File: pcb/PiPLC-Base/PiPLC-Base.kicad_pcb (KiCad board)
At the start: 2 copper layers, 158.9 x 85 mm, 139 parts, among them J1 WJ2EDGRC-5.08-4P, J10 WJ2EDGRC-5.08-4P, J11 WJ2EDGRC-5.08-4P, J12 WJ2EDGRC-5.08-4P, J13 ?, J2 KNX, J3 WJ2EDGRC-5.08-4P, J4 WJ2EDGRC-5.08-4P, J5 WJ2EDGRC-5.08-4P, J6 WJ2EDGRC-5.08-4P, J7 WJ2EDGRC-5.08-4P, J8 WJ2EDGRC-5.08-4P, J9 WJ2EDGRC-5.08-4P, J99 Rpi GPIO, K1 G5RL-1A-E-TV8 DC24, K2 G5RL-1A-E-TV8 DC24, K3 G5RL-1A-E-TV8 DC24, K4 G5RL-1A-E-TV8 DC24, K5 G5RL-1A-E-TV8 DC24, K6 G5RL-1A-E-TV8 DC24, K7 G5RL-1A-E-TV8 DC24, K8 G5RL-1A-E-TV8 DC24, Q1 AO3400A, Q2 AO3400A, Q3 AO3400A, Q4 AO3400A, Q5 AO3400A, Q6 AO3400A, Q7 AO3400A, Q8 AO3400A, U1 TPS54331D, U10 EL817C, U11 EL817C, U2 NCN5121, U3 ISO1540, U4 EL817C, U5 EL817C, U6 EL817C, U7 EL817C, U8 EL817C, U9 EL817C, Y1 16MHz

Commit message: Add 3D files for MSTB plugs
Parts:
- moved C16 0.45 mm to (-8.26, 140.8)
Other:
- board size 158.9 x 85 mm -> 158 x 85 mm
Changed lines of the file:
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@@
   (setup
     (pad_to_mask_clearance 0)
+    (aux_axis_origin 66.04 63.5)
     (grid_origin 66.04 63.5)
     (pcbplotparams
@@
       (rotate (xyz 0 0 0))
     )
+    (model "${MEINE_BIBS}/MeineBib.3dshapes/PhoenixContact_MSTB_2,5⁄ 4-ST-5,08.stp"
+      (offset (xyz -2.5 -19.8 0))
+      (scale (xyz 1 1 1))
+      (rotate (xyz 0 0 0))
+    )
   )
   (footprint "Relay_THT:Relay_SPST_Omron_G2RL-1A-E" (layer "F.Cu")
@@
   )
   (footprint "Capacitor_SMD:CP_Elec_6.3x7.7" (layer "F.Cu")
-    (at -8.149 140.366)
+    (at -8.26 140.8)
     (descr "SMD capacitor, aluminum electrolytic, Nichicon, 6.3x7.7mm")
     (tags "capacitor electrolytic")
@@
       (rotate (xyz 0 0 0))
     )
+    (model "${MEINE_BIBS}/MeineBib.3dshapes/PhoenixContact_MSTB_2,5⁄ 4-ST-5,08.stp"
+      (offset (xyz -2.5 -19.8 0))
+      (scale (xyz 1 1 1))
+      (rotate (xyz 0 0 0))
+    )
   )
   (footprint "Resistor_SMD:R_0603_1608Metric" (layer "F.Cu")
@@
       (rotate (xyz 0 0 0))
     )
+    (model "${MEINE_BIBS}/MeineBib.3dshapes/PhoenixContact_MSTB_2,5⁄ 4-ST-5,08.stp"
+      (offset (xyz -2.5 -19.8 0))
+      (scale (xyz 1 1 1))
+      (rotate (xyz 0 0 0))
+    )
   )
   (footprint "Resistor_SMD:R_0603_1608Metric" (layer "F.Cu")
@@
       (rotate (xyz 0 0 0))
     )
+    (model "${MEINE_BIBS}/MeineBib.3dshapes/PhoenixContact_MSTB_2,5⁄ 4-ST-5,08.stp"
+      (offset (xyz -2.5 -19.8 0))
+      (scale (xyz 1 1 1))
+      (rotate (xyz 0 0 0))
+    )
   )
   (footprint "MeineBib:Optocoupler_DIP_S1" (layer "F.Cu")
@@
       (rotate (xyz 0 0 0))
     )
+    (model "${MEINE_BIBS}/MeineBib.3dshapes/PhoenixContact_MSTB_2,5⁄ 4-ST-5,08.stp"
+      (offset (xyz -2.5 -19.8 0))
+      (scale (xyz 1 1 1))
+      (rotate (xyz 0 0 0))
+    )
   )
   (footprint "LED_THT:LED_D5.0mm" (layer "F.Cu")
@@
       (rotate (xyz 0 0 0))
     )
+    (model "${MEINE_BIBS}/MeineBib.3dshapes/PhoenixContact_MSTB_2,5⁄ 4-ST-5,08.stp"
+      (offset (xyz -2.5 -19.8 0))
+      (scale (xyz 1 1 1))
+      (rotate (xyz 0 0 0))
+    )
   )
   (footprint "Relay_THT:Relay_SPST_Omron_G2RL-1A-E" (layer "F.Cu")
@@
       (rotate (xyz 0 0 0))
     )
+    (model "${MEINE_BIBS}/MeineBib.3dshapes/PhoenixContact_MSTB_2,5⁄ 4-ST-5,08.stp"
+      (offset (xyz -2.5 -19.8 0))
+      (scale (xyz 1 1 1))
+      (rotate (xyz 0 0 0))
+    )
   )
   (footprint "Capacitor_SMD:C_0603_1608Metric" (layer "F.Cu")
@@
       (rotate (xyz 0 0 0))
     )
+    (model "${MEINE_BIBS}/MeineBib.3dshapes/PhoenixContact_MSTB_2,5⁄ 4-ST-5,08.stp"
+      (offset (xyz -2.5 -19.8 0))
+      (scale (xyz 1 1 1))
+      (rotate (xyz 0 0 0))
+    )
   )
   (footprint "Resistor_SMD:R_0603_1608Metric" (layer "F.Cu")
@@
     )
     (model "${MEINE_BIBS}/MeineBib.3dshapes/Raspberry Pi 4 Model B.STEP"
-      (offset (xyz -25.77 -14.15 25))
+      (offset (xyz -25.77 -14.15 35))
       (scale (xyz 1 1 1))
       (rotate (xyz 90 0 -90))
@@
       (rotate (xyz 0 0 0))
     )
+    (model "${MEINE_BIBS}/MeineBib.3dshapes/PhoenixContact_MSTB_2,5⁄ 4-ST-5,08.stp"
+      (offset (xyz -2.5 -19.8 0))
+      (scale (xyz 1 1 1))
+      (rotate (xyz 0 0 0))
+    )
   )
   (footprint "Resistor_SMD:R_1206_3216Metric" (layer "F.Cu")
@@
       (rotate (xyz 0 0 0))
     )
+    (model "${MEINE_BIBS}/MeineBib.3dshapes/PhoenixContact_MSTB_2,5⁄ 4-ST-5,08.stp"
+      (offset (xyz -2.5 -19.8 0))
+      (scale (xyz 1 1 1))
+      (rotate (xyz 0 0 0))
+    )
   )
   (footprint "Capacitor_SMD:C_0603_1608Metric" (layer "F.Cu")
@@
       (rotate (xyz 0 0 0))
     )
+    (model "${MEINE_BIBS}/MeineBib.3dshapes/PhoenixContact_MSTB_2,5⁄ 4-ST-5,08.stp"
+      (offset (xyz -2.5 -19.8 0))
+      (scale (xyz 1 1 1))
+      (rotate (xyz 0 0 0))
+    )
   )
   (footprint "Resistor_SMD:R_0603_1608Metric" (layer "F.Cu")
@@
       (rotate (xyz 0 0 0))
     )
+    (model "${MEINE_BIBS}/MeineBib.3dshapes/PhoenixContact_MSTB_2,5⁄ 4-ST-5,08.stp"
+      (offset (xyz -2.5 -19.8 0))
+      (scale (xyz 1 1 1))
+      (rotate (xyz 0 0 0))
+    )
   )
   (footprint "LED_THT:LED_D5.0mm" (layer "F.Cu")
@@
     )
   )
-  (gr_rect (start 66.04 63.5) (end 224.94 148.5)
+  (gr_rect (start 66.04 63.5) (end 224.04 148.5)
     (stroke (width 0.1) (type default)) (fill none) (layer "Edge.Cuts"))
 )

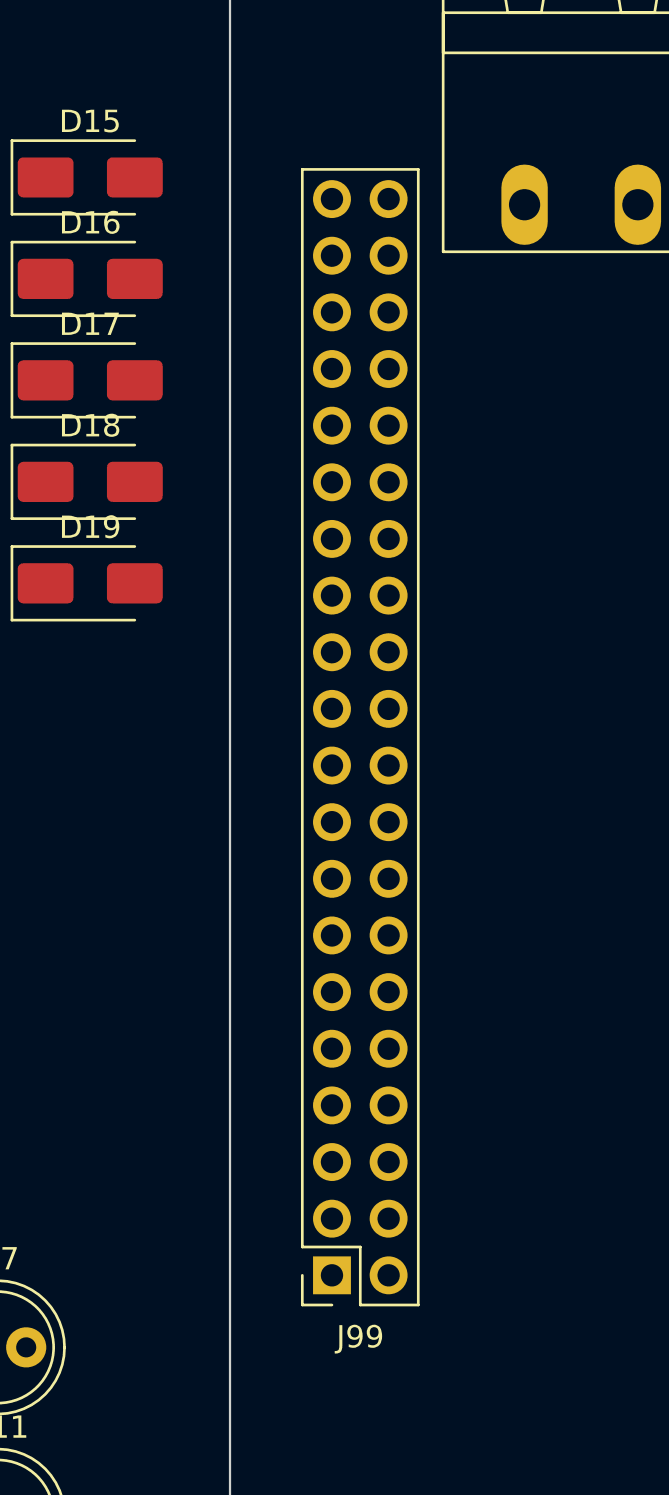
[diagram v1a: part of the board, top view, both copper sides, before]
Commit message: Move Pi to align outer edges of PCBs
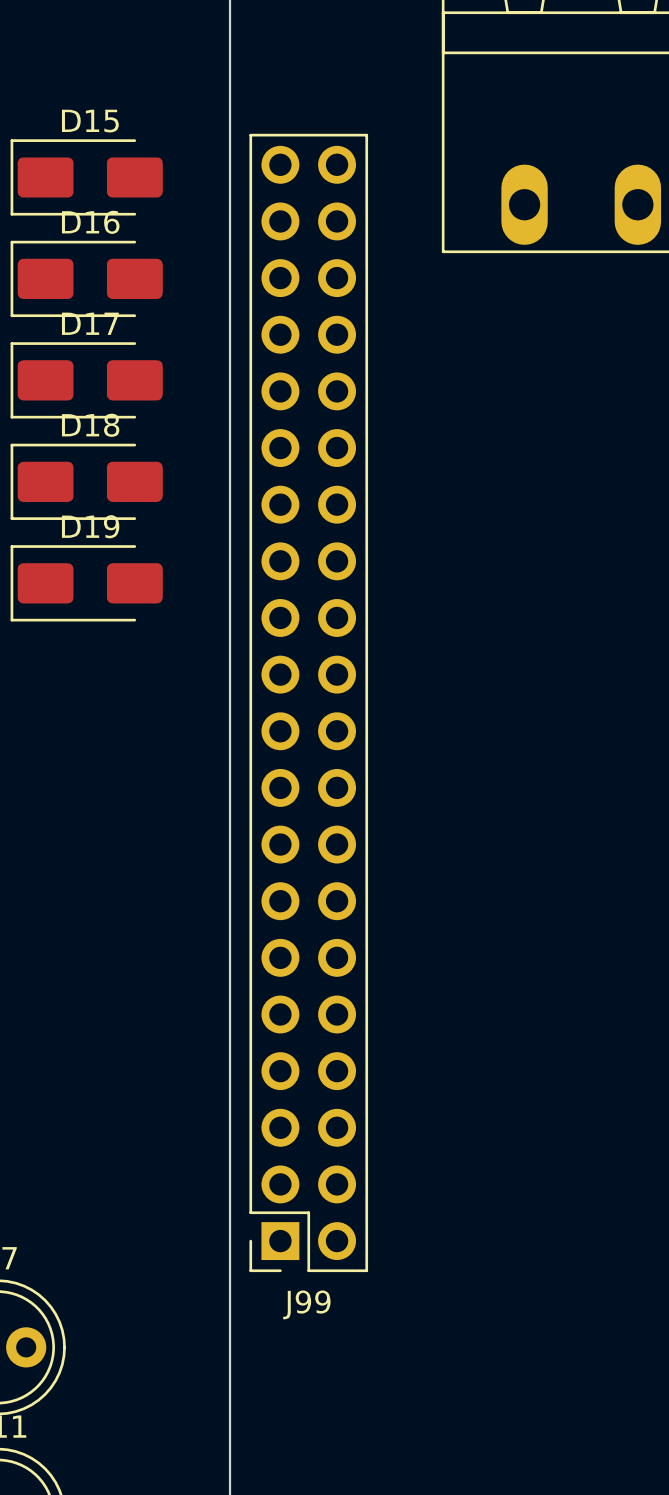
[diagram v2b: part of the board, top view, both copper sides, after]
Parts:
- added RP?: Raspberry_Pi_2_3, Rpi:raspberrypi_2_3, B.Cu at (69.6, 96.0)
- moved J99 2.78 mm to (68.3, 120.1)
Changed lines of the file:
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@@
   )
   (footprint "Connector_PinSocket_2.54mm:PinSocket_2x20_P2.54mm_Vertical" (layer "F.Cu")
-    (at 70.612 121.666 180)
+    (at 68.3 120.13 180)
     (descr "Through hole straight socket strip, 2x20, 2.54mm pitch, double cols (from Kicad 4.0.7), script generated")
     (tags "Through hole socket strip THT 2x20 2.54mm double row")
@@
     )
     (model "${MEINE_BIBS}/MeineBib.3dshapes/Raspberry Pi 4 Model B.STEP"
-      (offset (xyz -25.77 -14.15 35))
+      (offset (xyz -25.77 -14.15 32.8))
       (scale (xyz 1 1 1))
       (rotate (xyz 90 0 -90))
@@
     )
   )
+  (footprint "Rpi:raspberrypi_2_3" (layer "B.Cu")
+    (at 69.57 96 -90)
+    (descr "RaspberryPi 2")
+    (tags "CONN")
+    (attr through_hole board_only exclude_from_pos_files exclude_from_bom allow_missing_courtyard)
+    (fp_text reference "RP?" (at 0 8.9 90) (layer "B.Fab")
+        (effects (font (size 2 2) (thickness 0.25)) (justify mirror))
+    )
+    (fp_text value "Raspberry_Pi_2_3" (at 0.1 5.7 90) (layer "B.Fab")
+        (effects (font (size 2 2) (thickness 0.25)) (justify mirror))
+    )
+    (fp_text user "By Lukaneco" (at 23.7 6.8 90) (layer "B.Fab")
+        (effects (font (size 1 1) (thickness 0.15)) (justify mirror))
+    )
+    (fp_line (start -32.5 -16.4) (end -32.5 -31)
+      (stroke (width 0.15) (type solid)) (layer "F.CrtYd"))
+    (fp_line (start -25.7 -52.5) (end -25.7 -47.5)
+      (stroke (width 0.15) (type solid)) (layer "F.CrtYd"))
+    (fp_line (start -18.2 -52.5) (end -25.7 -52.5)
+      (stroke (width 0.15) (type solid)) (layer "F.CrtYd"))
+    (fp_line (start -18.2 -52.5) (end -18.2 -47.5)
+      (stroke (width 0.15) (type solid)) (layer "F.CrtYd"))
+    (fp_line (start -18.2 -47.5) (end -25.7 -47.5)
+      (stroke (width 0.15) (type solid)) (layer "F.CrtYd"))
+    (fp_line (start -17.9 -31) (end -32.5 -31)
+      (stroke (width 0.15) (type solid)) (layer "F.CrtYd"))
+    (fp_line (start -17.9 -16.4) (end -32.5 -16.4)
+      (stroke (width 0.15) (type solid)) (layer "F.CrtYd"))
+    (fp_line (start -17.9 -16.4) (end -17.9 -31)
+      (stroke (width 0.15) (type solid)) (layer "F.CrtYd"))
+    (fp_line (start -8 -41.8) (end -8 -52.5)
+      (stroke (width 0.15) (type solid)) (layer "F.CrtYd"))
+    (fp_line (start -8 -41.8) (end 7 -41.8)
+      (stroke (width 0.15) (type solid)) (layer "F.CrtYd"))
+    (fp_line (start 7 -52.5) (end -8 -52.5)
+      (stroke (width 0.15) (type solid)) (layer "F.CrtYd"))
+    (fp_line (start 7 -52.5) (end 7 -41.8)
+      (stroke (width 0.15) (type solid)) (layer "F.CrtYd"))
+    (fp_line (start 18 -55) (end 24 -55)
+      (stroke (width 0.15) (type solid)) (layer "F.CrtYd"))
+    (fp_line (start 18 -37) (end 18 -55)
+      (stroke (width 0.15) (type solid)) (layer "F.CrtYd"))
+    (fp_line (start 24 -55) (end 24 -37)
+      (stroke (width 0.15) (type solid)) (layer "F.CrtYd"))
+    (fp_line (start 24 -37) (end 18 -37)
+      (stroke (width 0.15) (type solid)) (layer "F.CrtYd"))
+    (fp_line (start 33.6 -50.2) (end 33.6 -34.3)
+      (stroke (width 0.15) (type solid)) (layer "F.CrtYd"))
+    (fp_line (start 33.6 -34.3) (end 54.6 -34.3)
+      (stroke (width 0.15) (type solid)) (layer "F.CrtYd"))
+    (fp_line (start 37.5 -30.1) (end 37.5 -17)
+      (stroke (width 0.15) (type solid)) (layer "F.CrtYd"))
+    (fp_line (start 37.5 -17) (end 54.6 -17)
+      (stroke (width 0.15) (type solid)) (layer "F.CrtYd"))
+    (fp_line (start 37.5 1) (end 37.5 -12.1)
+      (stroke (width 0.15) (type solid)) (layer "F.CrtYd"))
+    (fp_line (start 37.5 1) (end 54.6 1)
+      (stroke (width 0.15) (type solid)) (layer "F.CrtYd"))
+    (fp_line (start 54.6 -50.2) (end 33.6 -50.2)
+      (stroke (width 0.15) (type solid)) (layer "F.CrtYd"))
+    (fp_line (start 54.6 -50.2) (end 54.6 -34.3)
+      (stroke (width 0.15) (type solid)) (layer "F.CrtYd"))
+    (fp_line (start 54.6 -30.1) (end 37.5 -30.1)
+      (stroke (width 0.15) (type solid)) (layer "F.CrtYd"))
+    (fp_line (start 54.6 -30.1) (end 54.6 -17)
+      (stroke (width 0.15) (type solid)) (layer "F.CrtYd"))
+    (fp_line (start 54.6 -12.1) (end 37.5 -12.1)
+      (stroke (width 0.15) (type solid)) (layer "F.CrtYd"))
+    (fp_line (start 54.6 -12.1) (end 54.6 1)
+      (stroke (width 0.15) (type solid)) (layer "F.CrtYd"))
+    (fp_line (start -32.5 -49) (end -32.5 0)
+      (stroke (width 0.15) (type solid)) (layer "B.Fab"))
+    (fp_line (start -29 -52.5) (end 49.5 -52.5)
+      (stroke (width 0.15) (type solid)) (layer "B.Fab"))
+    (fp_line (start -25.4 2.54) (end -25.4 -2.54)
+      (stroke (width 0.15) (type solid)) (layer "B.Fab"))
+    (fp_line (start -25.4 2.54) (end 25.4 2.54)
+      (stroke (width 0.15) (type solid)) (layer "B.Fab"))
+    (fp_line (start 25.39492 -2.54) (end 25.39492 2.54)
+      (stroke (width 0.15) (type solid)) (layer "B.Fab"))
+    (fp_line (start 25.4 -2.54) (end -25.4 -2.54)
+      (stroke (width 0.15) (type solid)) (layer "B.Fab"))
+    (fp_line (start 49.5 3.5) (end -29 3.5)
+      (stroke (width 0.15) (type solid)) (layer "B.Fab"))
+    (fp_line (start 52.5 -49.5) (end 52.5 0.5)
+      (stroke (width 0.15) (type solid)) (layer "B.Fab"))
+    (fp_arc (start -32.5 -49) (mid -31.474874 -51.474874) (end -29 -52.5)
+      (stroke (width 0.15) (type solid)) (layer "B.Fab"))
+    (fp_arc (start -29 3.5) (mid -31.474874 2.474874) (end -32.5 0)
+      (stroke (width 0.15) (type solid)) (layer "B.Fab"))
+    (fp_arc (start 49.5 -52.5) (mid 51.62132 -51.62132) (end 52.5 -49.5)
+      (stroke (width 0.15) (type solid)) (layer "B.Fab"))
+    (fp_arc (start 52.5 0.5) (mid 51.62132 2.62132) (end 49.5 3.5)
+      (stroke (width 0.15) (type solid)) (layer "B.Fab"))
+    (model "unsorted/raspberryPi3b-simple.wrl"
+      (offset (xyz 9.905999851 -24.58719963 -18.28799973))
+      (scale (xyz 1 1 1))
+      (rotate (xyz 90 180 180))
+    )
+    (model "Pin_Header/Pin_Header_Straight_Female_2x20_RaspPi.wrl"
+      (offset (xyz 0 0 -6.349999905))
+      (scale (xyz 1 1 1))
+      (rotate (xyz 90 0 90))
+    )
+  )

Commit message: Move terminals around
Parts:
- added MK2: Mounting_Hole, MeineBib:EigenesMountingHole_3.2mm_M3_Small, F.Cu at (69.2, 145.3)
- added MK2: Mounting_Hole, MeineBib:EigenesMountingHole_3.2mm_M3_Small, F.Cu at (69.2, 66.7)
- added MK2: Mounting_Hole, MeineBib:EigenesMountingHole_3.2mm_M3_Small, F.Cu at (220.8, 66.7)
- added MK2: Mounting_Hole, MeineBib:EigenesMountingHole_3.2mm_M3_Small, F.Cu at (220.8, 145.3)
- moved J2 33.9 mm to (247.3, 126.6)
- moved J11 5.15 mm to (149.0, 140.4)
- moved J12 5.15 mm to (172.4, 140.4)
- moved J10 5.15 mm to (125.6, 140.4)
- moved J9 5.15 mm to (102.3, 140.4)
- moved J13 5.15 mm to (195.8, 140.4)
- moved J3 5.15 mm to (78.9, 140.4)
- moved J8 2.03 mm to (164.3, 71.7)
- moved J1 2.03 mm to (140.9, 71.7)
- moved J4 2.03 mm to (117.5, 71.7)
- moved J5 2.03 mm to (94.2, 71.7)
- moved J6 2.03 mm to (211.0, 71.7)
- moved J7 2.03 mm to (187.6, 71.7)
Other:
- outline, holes or cut-outs redrawn

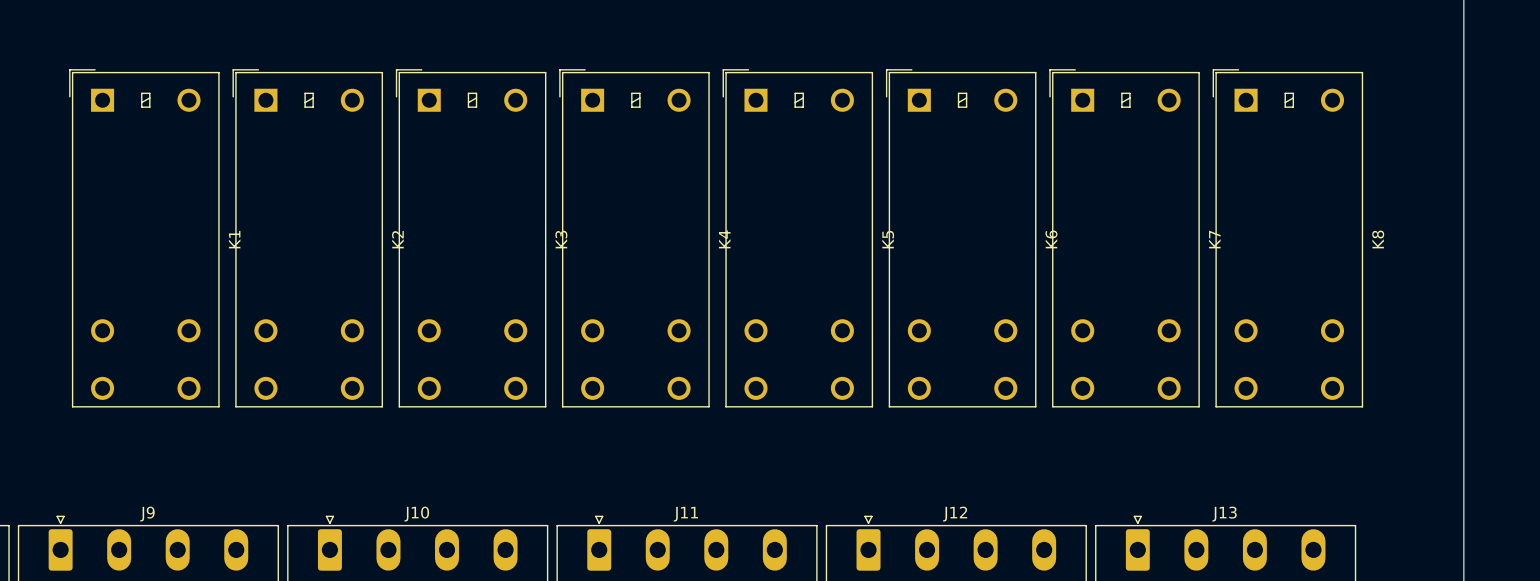
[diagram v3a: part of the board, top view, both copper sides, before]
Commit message: Split some parts of Mainboard off to Frontpanel
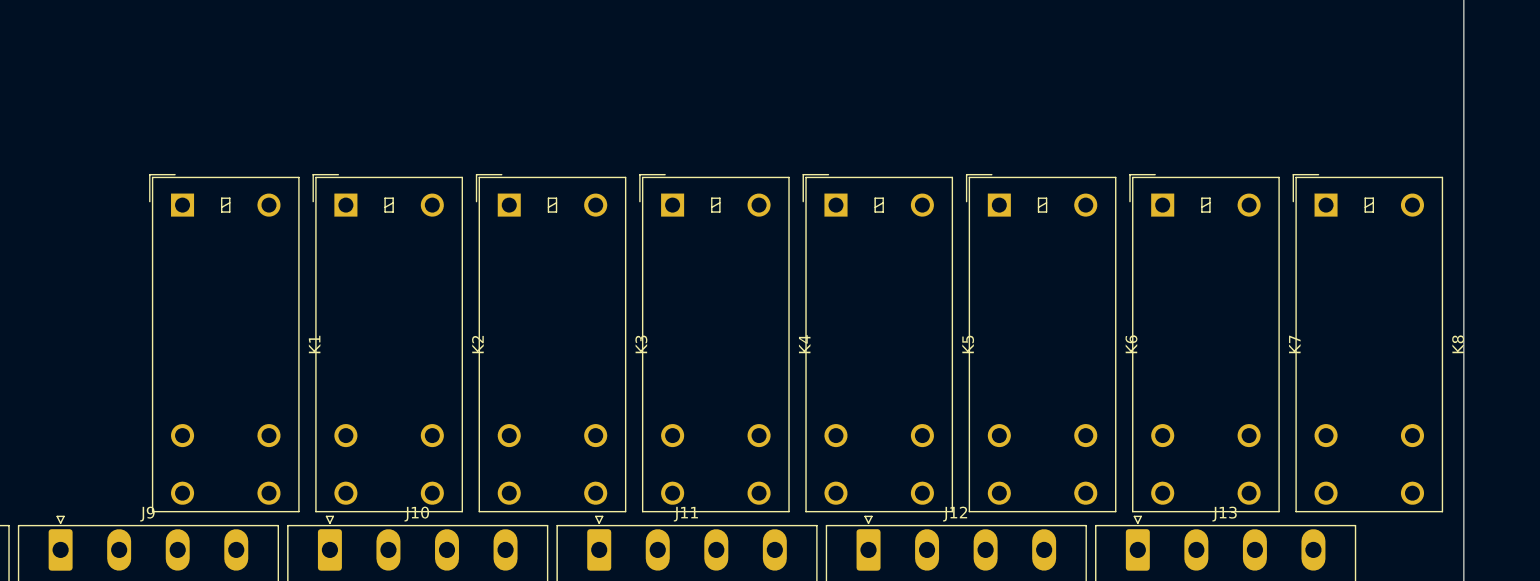
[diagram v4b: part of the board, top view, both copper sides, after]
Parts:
- moved K1 11.4 mm to (112.9, 110.5)
- moved K2 11.4 mm to (127.0, 110.5)
- moved K3 11.4 mm to (141.2, 110.5)
- moved K4 11.4 mm to (155.4, 110.5)
- moved K5 11.4 mm to (169.6, 110.5)
- moved K6 11.4 mm to (183.7, 110.5)
- moved K7 11.4 mm to (197.9, 110.5)
- moved K8 11.4 mm to (212.1, 110.5)
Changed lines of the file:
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@@
   )
   (footprint "Relay_THT:Relay_SPST_Omron_G2RL-1A-E" (layer "F.Cu")
-    (at 148.443 101.412)
+    (at 155.383 110.509)
     (descr "Omron Relay, SPST, High Capacity,  https://omronfs.omron.com/en_US/ecb/products/pdf/en-g2rl.pdf")
     (tags "Omron Relay SPST High Capacity")
@@
   )
   (footprint "Relay_THT:Relay_SPST_Omron_G2RL-1A-E" (layer "F.Cu")
-    (at 190.968 101.412)
+    (at 197.908 110.509)
     (descr "Omron Relay, SPST, High Capacity,  https://omronfs.omron.com/en_US/ecb/products/pdf/en-g2rl.pdf")
     (tags "Omron Relay SPST High Capacity")
@@
   )
   (footprint "Relay_THT:Relay_SPST_Omron_G2RL-1A-E" (layer "F.Cu")
-    (at 162.618 101.412)
+    (at 169.558 110.509)
     (descr "Omron Relay, SPST, High Capacity,  https://omronfs.omron.com/en_US/ecb/products/pdf/en-g2rl.pdf")
     (tags "Omron Relay SPST High Capacity")
@@
   )
   (footprint "Relay_THT:Relay_SPST_Omron_G2RL-1A-E" (layer "F.Cu")
-    (at 105.918 101.412)
+    (at 112.858 110.509)
     (descr "Omron Relay, SPST, High Capacity,  https://omronfs.omron.com/en_US/ecb/products/pdf/en-g2rl.pdf")
     (tags "Omron Relay SPST High Capacity")
@@
   )
   (footprint "Relay_THT:Relay_SPST_Omron_G2RL-1A-E" (layer "F.Cu")
-    (at 134.268 101.412)
+    (at 141.208 110.509)
     (descr "Omron Relay, SPST, High Capacity,  https://omronfs.omron.com/en_US/ecb/products/pdf/en-g2rl.pdf")
     (tags "Omron Relay SPST High Capacity")
@@
   )
   (footprint "Relay_THT:Relay_SPST_Omron_G2RL-1A-E" (layer "F.Cu")
-    (at 205.143 101.412)
+    (at 212.083 110.509)
     (descr "Omron Relay, SPST, High Capacity,  https://omronfs.omron.com/en_US/ecb/products/pdf/en-g2rl.pdf")
     (tags "Omron Relay SPST High Capacity")
@@
   )
   (footprint "Relay_THT:Relay_SPST_Omron_G2RL-1A-E" (layer "F.Cu")
-    (at 120.093 101.412)
+    (at 127.033 110.509)
     (descr "Omron Relay, SPST, High Capacity,  https://omronfs.omron.com/en_US/ecb/products/pdf/en-g2rl.pdf")
     (tags "Omron Relay SPST High Capacity")
@@
   )
   (footprint "Relay_THT:Relay_SPST_Omron_G2RL-1A-E" (layer "F.Cu")
-    (at 176.793 101.412)
+    (at 183.733 110.509)
     (descr "Omron Relay, SPST, High Capacity,  https://omronfs.omron.com/en_US/ecb/products/pdf/en-g2rl.pdf")
     (tags "Omron Relay SPST High Capacity")
